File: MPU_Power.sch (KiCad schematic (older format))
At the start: 2 parts

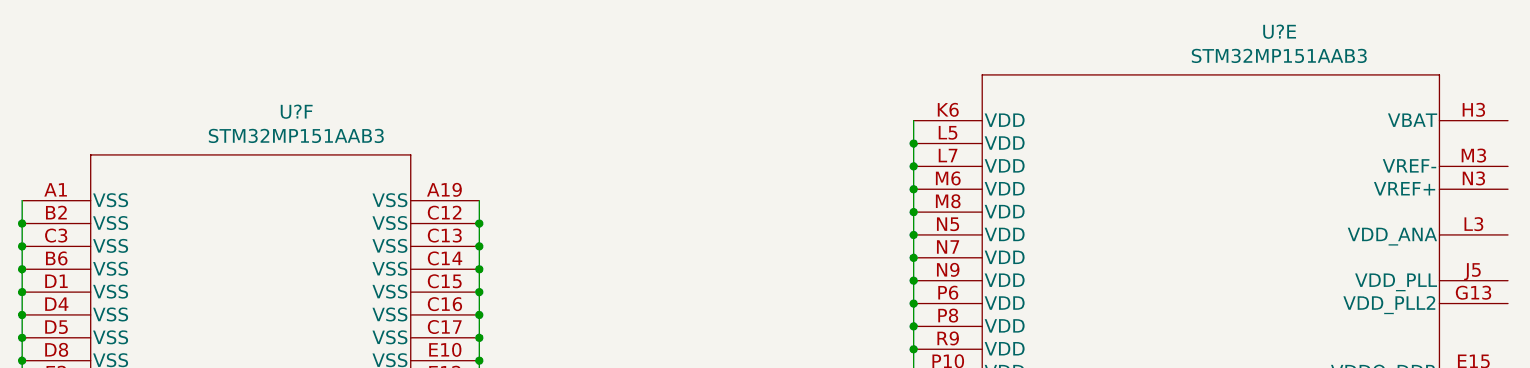
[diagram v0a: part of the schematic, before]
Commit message: Add bulk labels for RAM and ethernet
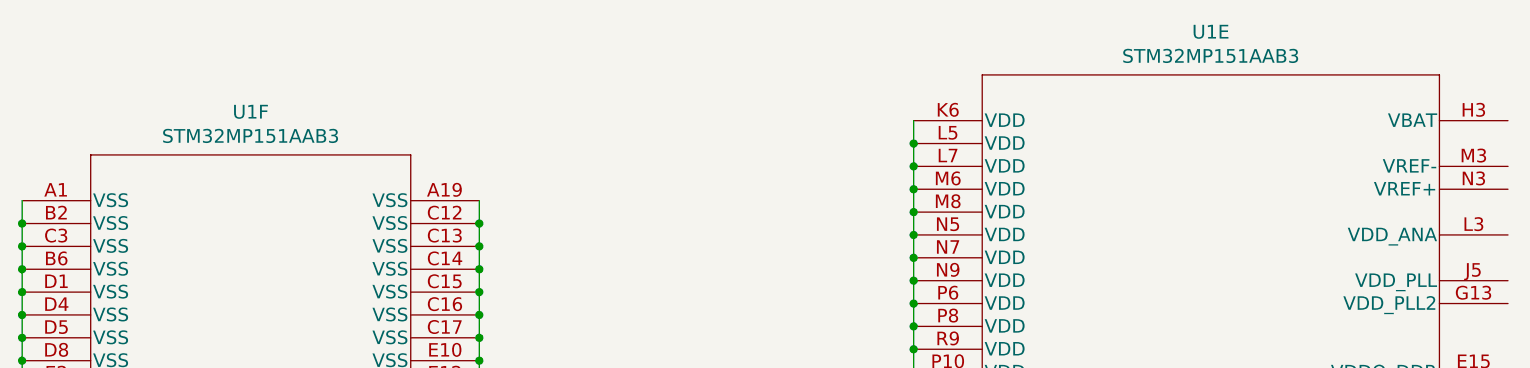
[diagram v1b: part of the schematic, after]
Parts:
- gave numbers to parts that had none: 1
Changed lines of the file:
@@
 P 2400 1400
 AR Path="/60172A77/60484461" Ref="U?"  Part="6"
-AR Path="/601728E9/60484461" Ref="U?"  Part="6"
-F 0 "U?" H 3600 1787 60  0000 C CNN
-F 1 "STM32MP151AAB3" H 3600 1681 60  0000 C CNN
+AR Path="/601728E9/60484461" Ref="U1"  Part="6"
+F 0 "U1" H 3400 1787 60  0000 C CNN
+F 1 "STM32MP151AAB3" H 3400 1681 60  0000 C CNN
 F 2 "LinuxBoard:STM32MP151AAB3" H 3400 1640 60  0001 C CNN
 F 3 "" H 2400 1400 60  0000 C CNN
@@
 P 6300 1050
 AR Path="/60172A77/60484467" Ref="U?"  Part="5"
-AR Path="/601728E9/60484467" Ref="U?"  Part="5"
-F 0 "U?" H 7900 1437 60  0000 C CNN
-F 1 "STM32MP151AAB3" H 7900 1331 60  0000 C CNN
+AR Path="/601728E9/60484467" Ref="U1"  Part="5"
+F 0 "U1" H 7600 1437 60  0000 C CNN
+F 1 "STM32MP151AAB3" H 7600 1331 60  0000 C CNN
 F 2 "LinuxBoard:STM32MP151AAB3" H 7300 1290 60  0001 C CNN
 F 3 "" H 6300 1050 60  0000 C CNN

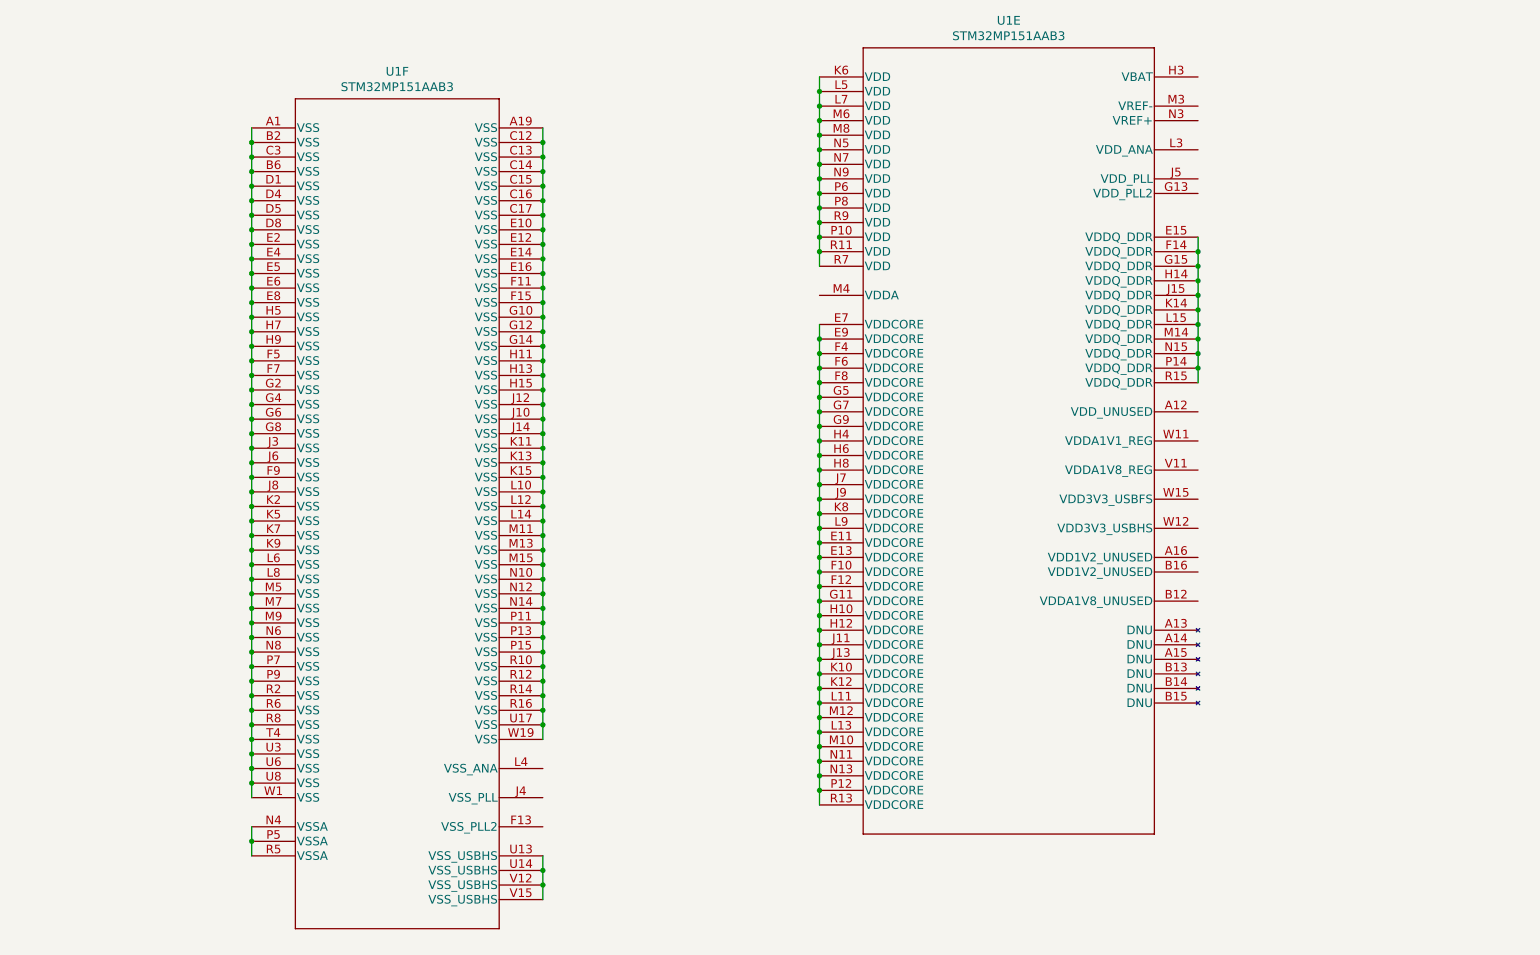
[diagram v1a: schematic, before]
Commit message: Add decoupling capacitors
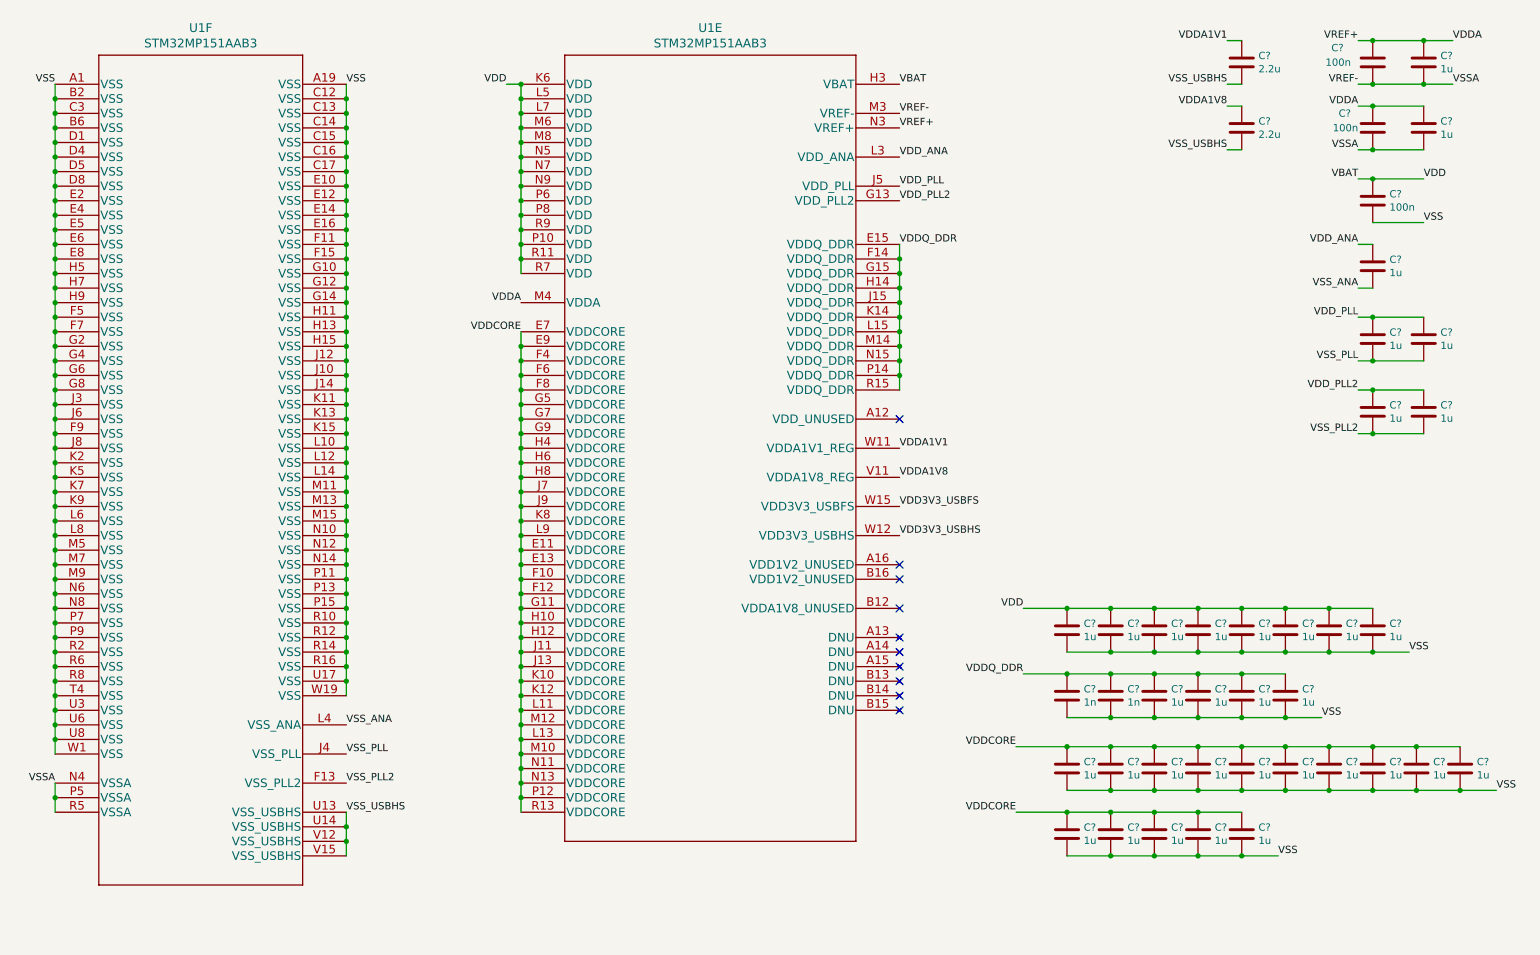
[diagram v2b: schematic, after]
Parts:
- added C? (x3): 100n, symbol Device:C
- added C? (x34): 1u, symbol Device:C
- added C? (x2): 1n, symbol Device:C
- added C? (x2): 2.2u, symbol Device:C
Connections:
- net VSS: now reaches U1.A1 (VSS), U1.B2 (VSS), U1.B6 (VSS), U1.C3 (VSS), U1.D1 (VSS), U1.D4 (VSS), U1.D5 (VSS), U1.D8 (VSS), U1.E2 (VSS), U1.E4 (VSS), U1.E5 (VSS), U1.E6 (VSS), U1.E8 (VSS), U1.F5 (VSS), U1.F7 (VSS), U1.F9 (VSS), U1.G2 (VSS), U1.G4 (VSS), U1.G6 (VSS), U1.G8 (VSS), U1.H5 (VSS), U1.H7 (VSS), U1.H9 (VSS), U1.J3 (VSS), U1.J6 (VSS), U1.J8 (VSS), U1.K2 (VSS), U1.K5 (VSS), U1.K7 (VSS), U1.K9 (VSS), U1.L6 (VSS), U1.L8 (VSS), U1.M5 (VSS), U1.M7 (VSS), U1.M9 (VSS), U1.N6 (VSS), U1.N8 (VSS), U1.P7 (VSS), U1.P9 (VSS), U1.R2 (VSS), U1.R6 (VSS), U1.R8 (VSS), U1.T4 (VSS), U1.U3 (VSS), U1.U6 (VSS), U1.U8 (VSS), U1.W1 (VSS)
- net VSS: now also U1.A19 (VSS), U1.C12 (VSS), U1.C13 (VSS), U1.C14 (VSS), U1.C15 (VSS), U1.C16 (VSS), U1.C17 (VSS), U1.E10 (VSS), U1.E12 (VSS), U1.E14 (VSS), U1.E16 (VSS), U1.F11 (VSS), U1.F15 (VSS), U1.G10 (VSS), U1.G12 (VSS), U1.G14 (VSS), U1.H11 (VSS), U1.H13 (VSS), U1.H15 (VSS), U1.J10 (VSS), U1.J12 (VSS), U1.J14 (VSS), U1.K11 (VSS), U1.K13 (VSS), U1.K15 (VSS), U1.L10 (VSS), U1.L12 (VSS), U1.L14 (VSS), U1.M11 (VSS), U1.M13 (VSS), U1.M15 (VSS), U1.N10 (VSS), U1.N12 (VSS), U1.N14 (VSS), U1.P11 (VSS), U1.P13 (VSS), U1.P15 (VSS), U1.R10 (VSS), U1.R12 (VSS), U1.R14 (VSS), U1.R16 (VSS), U1.U17 (VSS), U1.W19 (VSS), C?.2, C?.2, C?.2, C?.2, C?.2, C?.2, C?.2, C?.2, C?.2, C?.2, C?.2, C?.2, C?.2, C?.2, C?.2, C?.2, C?.2, C?.2, C?.2, C?.2, C?.2, C?.2, C?.2, C?.2, C?.2, C?.2, C?.2, C?.2, C?.2, C?.2
- net VSS_PLL2: now reaches U1.F13 (VSS_PLL2)
- net VSS_PLL2: now also C?.2, C?.2
- net VSS_PLL: now reaches U1.J4 (VSS_PLL)
- net VSS_PLL: now also C?.2, C?.2
- net VSS_ANA: now reaches U1.L4 (VSS_ANA)
- net VSS_ANA: now also C?.2
- net VREF-: now reaches U1.N4 (VSSA), U1.P5 (VSSA), U1.R5 (VSSA)
- net VREF-: now also U1.M3 (VREF-), C?.1, C?.1, C?.2, C?.2
- net VSS_USBHS: now reaches U1.U13 (VSS_USBHS), U1.U14 (VSS_USBHS), U1.V12 (VSS_USBHS), U1.V15 (VSS_USBHS)
- net VSS_USBHS: now also C?.2, C?.2
- net VDDCORE: now reaches U1.E11 (VDDCORE), U1.E13 (VDDCORE), U1.E7 (VDDCORE), U1.E9 (VDDCORE), U1.F10 (VDDCORE), U1.F12 (VDDCORE), U1.F4 (VDDCORE), U1.F6 (VDDCORE), U1.F8 (VDDCORE), U1.G11 (VDDCORE), U1.G5 (VDDCORE), U1.G7 (VDDCORE), U1.G9 (VDDCORE), U1.H10 (VDDCORE), U1.H12 (VDDCORE), U1.H4 (VDDCORE), U1.H6 (VDDCORE), U1.H8 (VDDCORE), U1.J11 (VDDCORE), U1.J13 (VDDCORE), U1.J7 (VDDCORE), U1.J9 (VDDCORE), U1.K10 (VDDCORE), U1.K12 (VDDCORE), U1.K8 (VDDCORE), U1.L11 (VDDCORE), U1.L13 (VDDCORE), U1.L9 (VDDCORE), U1.M10 (VDDCORE), U1.M12 (VDDCORE), U1.N11 (VDDCORE), U1.N13 (VDDCORE), U1.P12 (VDDCORE), U1.R13 (VDDCORE)
- net VDDCORE: now also C?.1, C?.1, C?.1, C?.1, C?.1, C?.1, C?.1, C?.1, C?.1, C?.1, C?.1, C?.1, C?.1, C?.1, C?.1
- net VDDQ_DDR: now reaches U1.E15 (VDDQ_DDR), U1.F14 (VDDQ_DDR), U1.G15 (VDDQ_DDR), U1.H14 (VDDQ_DDR), U1.J15 (VDDQ_DDR), U1.K14 (VDDQ_DDR), U1.L15 (VDDQ_DDR), U1.M14 (VDDQ_DDR), U1.N15 (VDDQ_DDR), U1.P14 (VDDQ_DDR), U1.R15 (VDDQ_DDR)
- net VDDQ_DDR: now also C?.1, C?.1, C?.1, C?.1, C?.1, C?.1
- net VDD_PLL2: now reaches U1.G13 (VDD_PLL2)
- net VDD_PLL2: now also C?.1, C?.1
- net VBAT: now reaches U1.H3 (VBAT)
- net VBAT: now also U1.K6 (VDD), U1.L5 (VDD), U1.L7 (VDD), U1.M6 (VDD), U1.M8 (VDD), U1.N5 (VDD), U1.N7 (VDD), U1.N9 (VDD), U1.P10 (VDD), U1.P6 (VDD), U1.P8 (VDD), U1.R11 (VDD), U1.R7 (VDD), U1.R9 (VDD), C?.1, C?.1, C?.1, C?.1, C?.1, C?.1, C?.1, C?.1, C?.1
- net VDD_PLL: now reaches U1.J5 (VDD_PLL)
- net VDD_PLL: now also C?.1, C?.1
- net VDD_ANA: now reaches U1.L3 (VDD_ANA)
- net VDD_ANA: now also C?.1
- net VDDA: now reaches U1.M4 (VDDA)
- net VDDA: now also U1.N3 (VREF+), C?.1, C?.1, C?.2, C?.2
- net VDDA1V8: now reaches U1.V11 (VDDA1V8_REG)
- net VDDA1V8: now also C?.1
- net VDDA1V1: now reaches U1.W11 (VDDA1V1_REG)
- net VDDA1V1: now also C?.1
- net VDD3V3_USBHS: now reaches U1.W12 (VDD3V3_USBHS)
- net VDD3V3_USBFS: now reaches U1.W15 (VDD3V3_USBFS)
- no-connect marks 0 -> 10
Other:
- moved on the sheet: U1E, U1F

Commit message: Finish labelling RAM
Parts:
- gave numbers to parts that had none: 41
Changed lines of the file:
@@
 VSSA
 $Comp
-L Device:C C?
+L Device:C C43
 U 1 1 607B0788
 P 10100 950
-F 0 "C?" H 10300 850 50  0000 L CNN
+F 0 "C43" H 10300 850 50  0000 L CNN
 F 1 "100n" H 10250 950 50  0000 L CNN
 F 2 "" H 10138 800 50  0001 C CNN
@@
 	10100 1100 10000 1100
 $Comp
-L Device:C C?
+L Device:C C52
 U 1 1 6094D435
 P 10450 950
-F 0 "C?" H 10565 996 50  0000 L CNN
+F 0 "C52" H 10565 996 50  0000 L CNN
 F 1 "1u" H 10565 905 50  0000 L CNN
 F 2 "" H 10488 800 50  0001 C CNN
@@
 VSSA
 $Comp
-L Device:C C?
+L Device:C C44
 U 1 1 609C619C
 P 10100 1400
-F 0 "C?" H 10250 1300 50  0000 L CNN
+F 0 "C44" H 10250 1300 50  0000 L CNN
 F 1 "100n" H 10200 1400 50  0000 L CNN
 F 2 "" H 10138 1250 50  0001 C CNN
@@
 	10100 1550 10000 1550
 $Comp
-L Device:C C?
+L Device:C C53
 U 1 1 609C61A7
 P 10450 1400
-F 0 "C?" H 10565 1446 50  0000 L CNN
+F 0 "C53" H 10565 1446 50  0000 L CNN
 F 1 "1u" H 10565 1355 50  0000 L CNN
 F 2 "" H 10488 1250 50  0001 C CNN
@@
 VDD
 $Comp
-L Device:C C?
+L Device:C C45
 U 1 1 60A08712
 P 10100 1900
-F 0 "C?" H 10215 1946 50  0000 L CNN
+F 0 "C45" H 10215 1946 50  0000 L CNN
 F 1 "100n" H 10215 1855 50  0000 L CNN
 F 2 "" H 10138 1750 50  0001 C CNN
@@
 VDDCORE
 $Comp
-L Device:C C?
+L Device:C C18
 U 1 1 60A31F57
 P 8000 5800
-F 0 "C?" H 8115 5846 50  0000 L CNN
+F 0 "C18" H 8115 5846 50  0000 L CNN
 F 1 "1u" H 8115 5755 50  0000 L CNN
 F 2 "" H 8038 5650 50  0001 C CNN
@@
 $EndComp
 $Comp
-L Device:C C?
+L Device:C C22
 U 1 1 60A5393A
 P 8300 5800
-F 0 "C?" H 8415 5846 50  0000 L CNN
+F 0 "C22" H 8415 5846 50  0000 L CNN
 F 1 "1u" H 8415 5755 50  0000 L CNN
 F 2 "" H 8338 5650 50  0001 C CNN
@@
 $EndComp
 $Comp
-L Device:C C?
+L Device:C C26
 U 1 1 60A5C6B0
 P 8600 5800
-F 0 "C?" H 8715 5846 50  0000 L CNN
+F 0 "C26" H 8715 5846 50  0000 L CNN
 F 1 "1u" H 8715 5755 50  0000 L CNN
 F 2 "" H 8638 5650 50  0001 C CNN
@@
 $EndComp
 $Comp
-L Device:C C?
+L Device:C C30
 U 1 1 60A653E0
 P 8900 5800
-F 0 "C?" H 9015 5846 50  0000 L CNN
+F 0 "C30" H 9015 5846 50  0000 L CNN
 F 1 "1u" H 9015 5755 50  0000 L CNN
 F 2 "" H 8938 5650 50  0001 C CNN
@@
 $EndComp
 $Comp
-L Device:C C?
+L Device:C C36
 U 1 1 60A6E191
 P 9200 5800
-F 0 "C?" H 9315 5846 50  0000 L CNN
+F 0 "C36" H 9315 5846 50  0000 L CNN
 F 1 "1u" H 9315 5755 50  0000 L CNN
 F 2 "" H 9238 5650 50  0001 C CNN
@@
 $EndComp
 $Comp
-L Device:C C?
+L Device:C C40
 U 1 1 60A76EB4
 P 9500 5800
-F 0 "C?" H 9615 5846 50  0000 L CNN
+F 0 "C40" H 9615 5846 50  0000 L CNN
 F 1 "1u" H 9615 5755 50  0000 L CNN
 F 2 "" H 9538 5650 50  0001 C CNN
@@
 $EndComp
 $Comp
-L Device:C C?
+L Device:C C42
 U 1 1 60A7FC09
 P 9800 5800
-F 0 "C?" H 9915 5846 50  0000 L CNN
+F 0 "C42" H 9915 5846 50  0000 L CNN
 F 1 "1u" H 9915 5755 50  0000 L CNN
 F 2 "" H 9838 5650 50  0001 C CNN
@@
 $EndComp
 $Comp
-L Device:C C?
+L Device:C C50
 U 1 1 60A888E7
 P 10100 5800
-F 0 "C?" H 10215 5846 50  0000 L CNN
+F 0 "C50" H 10215 5846 50  0000 L CNN
 F 1 "1u" H 10215 5755 50  0000 L CNN
 F 2 "" H 10138 5650 50  0001 C CNN
@@
 $EndComp
 $Comp
-L Device:C C?
+L Device:C C51
 U 1 1 60A91686
 P 10400 5800
-F 0 "C?" H 10515 5846 50  0000 L CNN
+F 0 "C51" H 10515 5846 50  0000 L CNN
 F 1 "1u" H 10515 5755 50  0000 L CNN
 F 2 "" H 10438 5650 50  0001 C CNN
@@
 $EndComp
 $Comp
-L Device:C C?
+L Device:C C56
 U 1 1 60A9A3BB
 P 10700 5800
-F 0 "C?" H 10815 5846 50  0000 L CNN
+F 0 "C56" H 10815 5846 50  0000 L CNN
 F 1 "1u" H 10815 5755 50  0000 L CNN
 F 2 "" H 10738 5650 50  0001 C CNN
@@
 	10400 5950 10700 5950
 $Comp
-L Device:C C?
+L Device:C C19
 U 1 1 60AD5BC4
 P 8000 6250
-F 0 "C?" H 8115 6296 50  0000 L CNN
+F 0 "C19" H 8115 6296 50  0000 L CNN
 F 1 "1u" H 8115 6205 50  0000 L CNN
 F 2 "" H 8038 6100 50  0001 C CNN
@@
 $EndComp
 $Comp
-L Device:C C?
+L Device:C C23
 U 1 1 60AD5BCA
 P 8300 6250
-F 0 "C?" H 8415 6296 50  0000 L CNN
+F 0 "C23" H 8415 6296 50  0000 L CNN
 F 1 "1u" H 8415 6205 50  0000 L CNN
 F 2 "" H 8338 6100 50  0001 C CNN
@@
 $EndComp
 $Comp
-L Device:C C?
+L Device:C C27
 U 1 1 60AD5BD0
 P 8600 6250
-F 0 "C?" H 8715 6296 50  0000 L CNN
+F 0 "C27" H 8715 6296 50  0000 L CNN
 F 1 "1u" H 8715 6205 50  0000 L CNN
 F 2 "" H 8638 6100 50  0001 C CNN
@@
 $EndComp
 $Comp
-L Device:C C?
+L Device:C C31
 U 1 1 60AD5BD6
 P 8900 6250
-F 0 "C?" H 9015 6296 50  0000 L CNN
+F 0 "C31" H 9015 6296 50  0000 L CNN
 F 1 "1u" H 9015 6205 50  0000 L CNN
 F 2 "" H 8938 6100 50  0001 C CNN
@@
 $EndComp
 $Comp
-L Device:C C?
+L Device:C C37
 U 1 1 60AD5BDC
 P 9200 6250
-F 0 "C?" H 9315 6296 50  0000 L CNN
+F 0 "C37" H 9315 6296 50  0000 L CNN
 F 1 "1u" H 9315 6205 50  0000 L CNN
 F 2 "" H 9238 6100 50  0001 C CNN
@@
 VDDQ_DDR
 $Comp
-L Device:C C?
+L Device:C C17
 U 1 1 60B613FA
 P 8000 5300
-F 0 "C?" H 8115 5346 50  0000 L CNN
+F 0 "C17" H 8115 5346 50  0000 L CNN
 F 1 "1n" H 8115 5255 50  0000 L CNN
 F 2 "" H 8038 5150 50  0001 C CNN
@@
 $EndComp
 $Comp
-L Device:C C?
+L Device:C C21
 U 1 1 60B663B8
 P 8300 5300
-F 0 "C?" H 8415 5346 50  0000 L CNN
+F 0 "C21" H 8415 5346 50  0000 L CNN
 F 1 "1n" H 8415 5255 50  0000 L CNN
 F 2 "" H 8338 5150 50  0001 C CNN
@@
 $EndComp
 $Comp
-L Device:C C?
+L Device:C C25
 U 1 1 60B715C2
 P 8600 5300
-F 0 "C?" H 8715 5346 50  0000 L CNN
+F 0 "C25" H 8715 5346 50  0000 L CNN
 F 1 "1u" H 8715 5255 50  0000 L CNN
 F 2 "" H 8638 5150 50  0001 C CNN
@@
 $EndComp
 $Comp
-L Device:C C?
+L Device:C C29
 U 1 1 60B7EB01
 P 8900 5300
-F 0 "C?" H 9015 5346 50  0000 L CNN
+F 0 "C29" H 9015 5346 50  0000 L CNN
 F 1 "1u" H 9015 5255 50  0000 L CNN
 F 2 "" H 8938 5150 50  0001 C CNN
@@
 $EndComp
 $Comp
-L Device:C C?
+L Device:C C35
 U 1 1 60B88EC8
 P 9200 5300
-F 0 "C?" H 9315 5346 50  0000 L CNN
+F 0 "C35" H 9315 5346 50  0000 L CNN
 F 1 "1u" H 9315 5255 50  0000 L CNN
 F 2 "" H 9238 5150 50  0001 C CNN
@@
 $EndComp
 $Comp
-L Device:C C?
+L Device:C C39
 U 1 1 60B9334D
 P 9500 5300
-F 0 "C?" H 9615 5346 50  0000 L CNN
+F 0 "C39" H 9615 5346 50  0000 L CNN
 F 1 "1u" H 9615 5255 50  0000 L CNN
 F 2 "" H 9538 5150 50  0001 C CNN
@@
 VSS_ANA
 $Comp
-L Device:C C?
+L Device:C C46
 U 1 1 60D502DF
 P 10100 2350
-F 0 "C?" H 10215 2396 50  0000 L CNN
+F 0 "C46" H 10215 2396 50  0000 L CNN
 F 1 "1u" H 10215 2305 50  0000 L CNN
 F 2 "" H 10138 2200 50  0001 C CNN
@@
 VSS_PLL
 $Comp
-L Device:C C?
+L Device:C C47
 U 1 1 60D6CA58
 P 10100 2850
-F 0 "C?" H 10215 2896 50  0000 L CNN
+F 0 "C47" H 10215 2896 50  0000 L CNN
 F 1 "1u" H 10215 2805 50  0000 L CNN
 F 2 "" H 10138 2700 50  0001 C CNN
@@
 VSS_PLL2
 $Comp
-L Device:C C?
+L Device:C C48
 U 1 1 60D8296D
 P 10100 3350
-F 0 "C?" H 10215 3396 50  0000 L CNN
+F 0 "C48" H 10215 3396 50  0000 L CNN
 F 1 "1u" H 10215 3305 50  0000 L CNN
 F 2 "" H 10138 3200 50  0001 C CNN
@@
 	10000 3500 10100 3500
 $Comp
-L Device:C C?
+L Device:C C16
 U 1 1 60DA2B65
 P 8000 4850
-F 0 "C?" H 8115 4896 50  0000 L CNN
+F 0 "C16" H 8115 4896 50  0000 L CNN
 F 1 "1u" H 8115 4805 50  0000 L CNN
 F 2 "" H 8038 4700 50  0001 C CNN
@@
 $EndComp
 $Comp
-L Device:C C?
+L Device:C C20
 U 1 1 60DA2B6B
 P 8300 4850
-F 0 "C?" H 8415 4896 50  0000 L CNN
+F 0 "C20" H 8415 4896 50  0000 L CNN
 F 1 "1u" H 8415 4805 50  0000 L CNN
 F 2 "" H 8338 4700 50  0001 C CNN
@@
 $EndComp
 $Comp
-L Device:C C?
+L Device:C C24
 U 1 1 60DA2B71
 P 8600 4850
-F 0 "C?" H 8715 4896 50  0000 L CNN
+F 0 "C24" H 8715 4896 50  0000 L CNN
 F 1 "1u" H 8715 4805 50  0000 L CNN
 F 2 "" H 8638 4700 50  0001 C CNN
@@
 $EndComp
 $Comp
-L Device:C C?
+L Device:C C28
 U 1 1 60DA2B77
 P 8900 4850
-F 0 "C?" H 9015 4896 50  0000 L CNN
+F 0 "C28" H 9015 4896 50  0000 L CNN
 F 1 "1u" H 9015 4805 50  0000 L CNN
 F 2 "" H 8938 4700 50  0001 C CNN
@@
 VDD
 $Comp
-L Device:C C?
+L Device:C C54
 U 1 1 60DE441F
 P 10450 2850
-F 0 "C?" H 10565 2896 50  0000 L CNN
+F 0 "C54" H 10565 2896 50  0000 L CNN
 F 1 "1u" H 10565 2805 50  0000 L CNN
 F 2 "" H 10488 2700 50  0001 C CNN
@@
 $EndComp
 $Comp
-L Device:C C?
+L Device:C C55
 U 1 1 60DEFD7A
 P 10450 3350
-F 0 "C?" H 10565 3396 50  0000 L CNN
+F 0 "C55" H 10565 3396 50  0000 L CNN
 F 1 "1u" H 10565 3305 50  0000 L CNN
 F 2 "" H 10488 3200 50  0001 C CNN
@@
 Connection ~ 10100 2700
 $Comp
-L Device:C C?
+L Device:C C34
 U 1 1 60E465D3
 P 9200 4850
-F 0 "C?" H 9315 4896 50  0000 L CNN
+F 0 "C34" H 9315 4896 50  0000 L CNN
 F 1 "1u" H 9315 4805 50  0000 L CNN
 F 2 "" H 9238 4700 50  0001 C CNN
@@
 $EndComp
 $Comp
-L Device:C C?
+L Device:C C38
 U 1 1 60E465D9
 P 9500 4850
-F 0 "C?" H 9615 4896 50  0000 L CNN
+F 0 "C38" H 9615 4896 50  0000 L CNN
 F 1 "1u" H 9615 4805 50  0000 L CNN
 F 2 "" H 9538 4700 50  0001 C CNN
@@
 $EndComp
 $Comp
-L Device:C C?
+L Device:C C41
 U 1 1 60E465DF
 P 9800 4850
-F 0 "C?" H 9915 4896 50  0000 L CNN
+F 0 "C41" H 9915 4896 50  0000 L CNN
 F 1 "1u" H 9915 4805 50  0000 L CNN
 F 2 "" H 9838 4700 50  0001 C CNN
@@
 $EndComp
 $Comp
-L Device:C C?
+L Device:C C49
 U 1 1 60E465E5
 P 10100 4850
-F 0 "C?" H 10215 4896 50  0000 L CNN
+F 0 "C49" H 10215 4896 50  0000 L CNN
 F 1 "1u" H 10215 4805 50  0000 L CNN
 F 2 "" H 10138 4700 50  0001 C CNN
@@
 VDDA1V1
 $Comp
-L Device:C C?
+L Device:C C32
 U 1 1 60E95E1E
 P 9200 950
-F 0 "C?" H 9315 996 50  0000 L CNN
+F 0 "C32" H 9315 996 50  0000 L CNN
 F 1 "2.2u" H 9315 905 50  0000 L CNN
 F 2 "" H 9238 800 50  0001 C CNN
@@
 VDDA1V8
 $Comp
-L Device:C C?
+L Device:C C33
 U 1 1 60F1B3A2
 P 9200 1400
-F 0 "C?" H 9315 1446 50  0000 L CNN
+F 0 "C33" H 9315 1446 50  0000 L CNN
 F 1 "2.2u" H 9315 1355 50  0000 L CNN
 F 2 "" H 9238 1250 50  0001 C CNN
